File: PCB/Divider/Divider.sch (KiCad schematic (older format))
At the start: 153 parts, among them U1 SFH617A-1

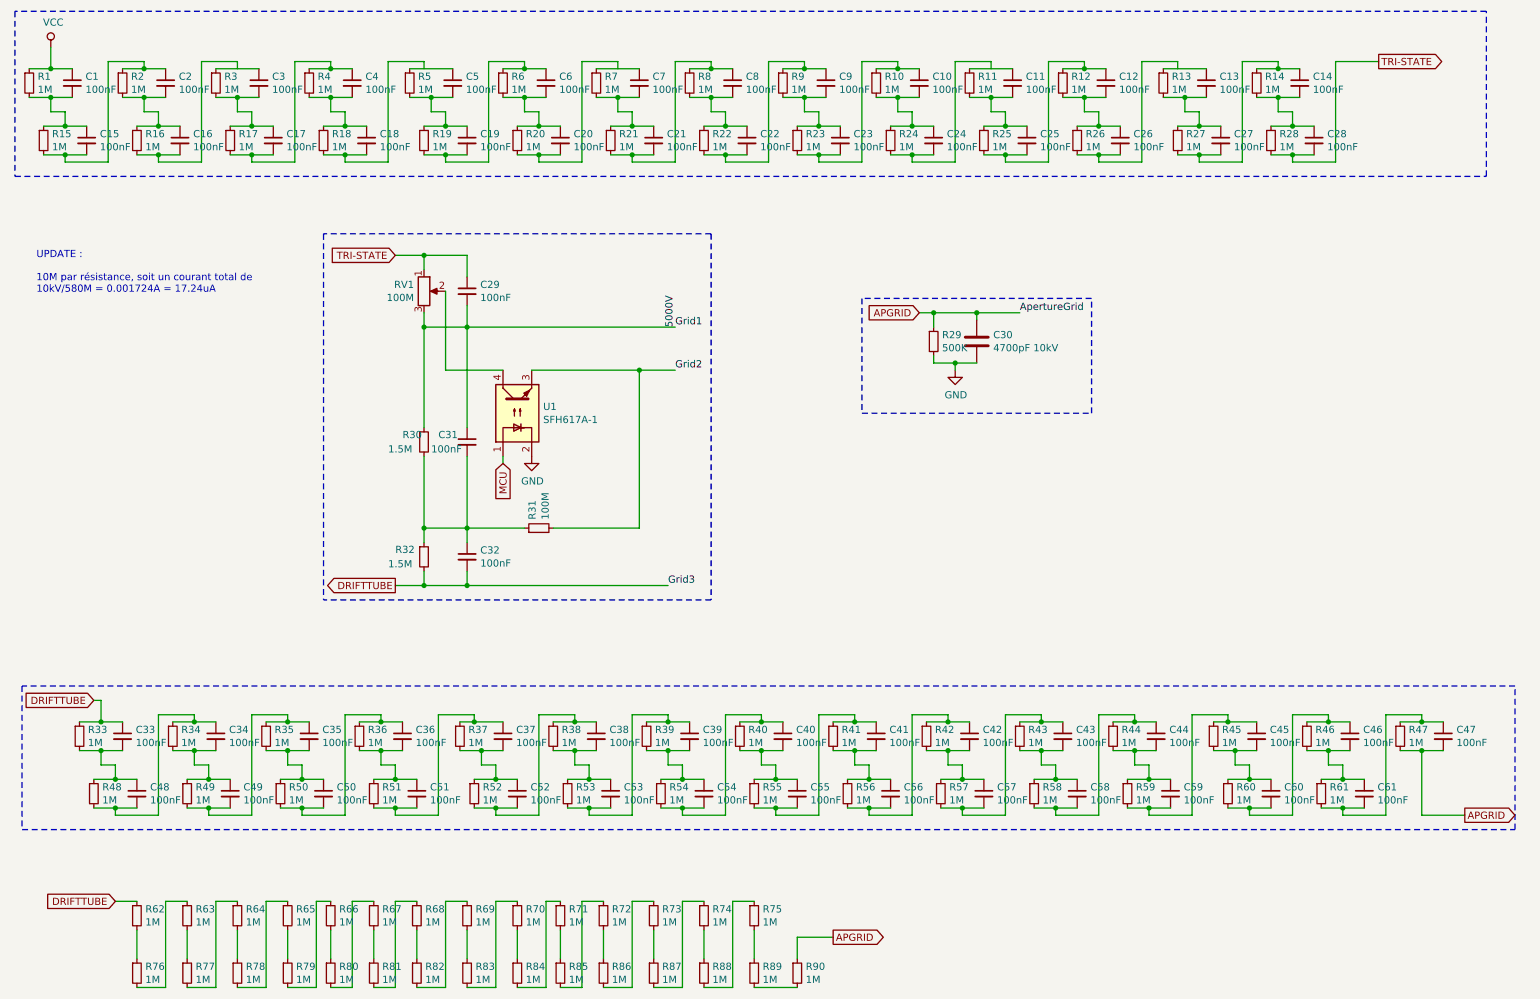
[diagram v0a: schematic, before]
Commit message: Begin PCB of divider
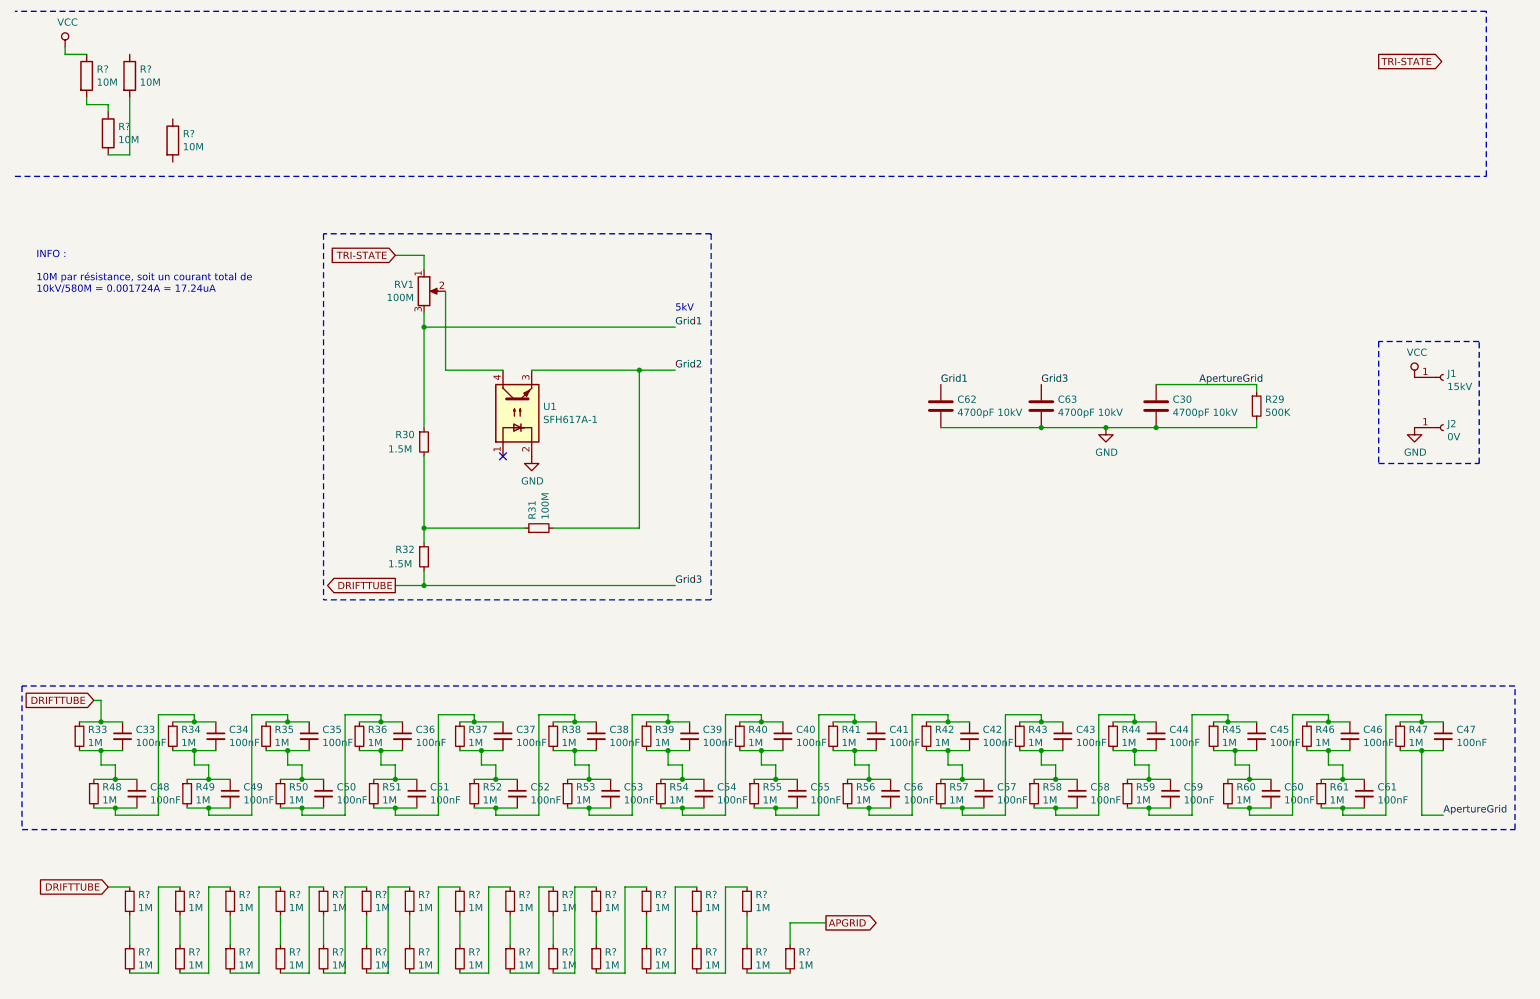
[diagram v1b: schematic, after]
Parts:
- removed C1, C10, C11, C12, C13, C14, C15, C16, C17, C18, C19, C2, C20, C21, C22, C23, C24, C25, C26, C27, C28, C29, C3, C31, C32, C4, C5, C6, C7, C8, C9: 100nF, symbol Device:C_Small
- removed R1, R10, R11, R12, R13, R14, R15, R16, R17, R18, R19, R2, R20, R21, R22, R23, R24, R25, R26, R27, R28, R3, R4, R5, R6, R62, R63, R64, R65, R66, R67, R68, R69, R7, R70, R71, R72, R73, R74, R75, R76, R77, R78, R79, R8, R80, R81, R82, R83, R84, R85, R86, R87, R88, R89, R9, R90: 1M, Resistor_SMD:R_1206_3216Metric, symbol Device:R_Small
- added C62, C63: 4700pF 10kV, Capacitor_THT:C_Rect_L13.0mm_W8.0mm_P10.00mm_FKS3_FKP3_MKS4, symbol Device:C
- added J1: 15kV, Connector_Pin:Pin_D1.4mm_L8.5mm_W2.8mm_FlatFork, symbol Connector:Conn_01x01_Female
- added J2: 0V, Connector_Pin:Pin_D1.4mm_L8.5mm_W2.8mm_FlatFork, symbol Connector:Conn_01x01_Female
- added R? (x29): 1M, Resistor_SMD:R_1206_3216Metric, symbol Device:R_Small
- added R? (x4): 10M, symbol Device:R
- C30: footprint Resistor_SMD:R_1206_3216Metric -> Capacitor_THT:C_Rect_L13.0mm_W8.0mm_P10.00mm_FKS3_FKP3_MKS4
- C33, C34, C35, C36, C37, C38, C39, C40, C41, C42, C43, C44, C45, C46, C47, C48, C49, C50, C51, C52, C53, C54, C55, C56, C57, C58, C59, C60, C61: footprint (none) -> Capacitor_SMD:C_1206_3216Metric
- RV1: footprint Potentiometer_THT:Potentiometer_ACP_CA6-H2,5_Horizontal -> Potentiometer_THT:Potentiometer_ACP_CA14-H4_Horizontal
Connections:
- net APGRID: now also R?.1; no longer C30.1, C47.2, R29.1, R47.2
- net DRIFTTUBE: now also C63.1, R?.1
- net GND: now also C62.2, C63.2, J2.1 (Pin_1)
- net VCC: now also J1.1 (Pin_1), R?.1
- net 5000V renamed Grid1
- net Grid1: now also C62.1
- net MCU: no longer names the net of U1.1
- new net: R?.2, R?.2 (x2)
- new net: R?.1, R?.2 (x28)
- new net ApertureGrid: C30.1, C47.2, R29.1, R47.2
- no-connect marks 0 -> 1
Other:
- note added: "5kV"
- note added: "INFO : \n\n10M par résistance, soit un courant total de \n10kV/580M = 0.001724A = 17.24uA\n\n"
- note removed: "UPDATE : \n\n10M par résistance, soit un courant total de \n10kV/580M = 0.001724A = 17.24uA\n\n"
- moved on the sheet: C30, R29
